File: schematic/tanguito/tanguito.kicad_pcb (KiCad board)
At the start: 2 copper layers, 10 parts, among them J1 Barrel_Jack, U2 L298N, U3 L298N

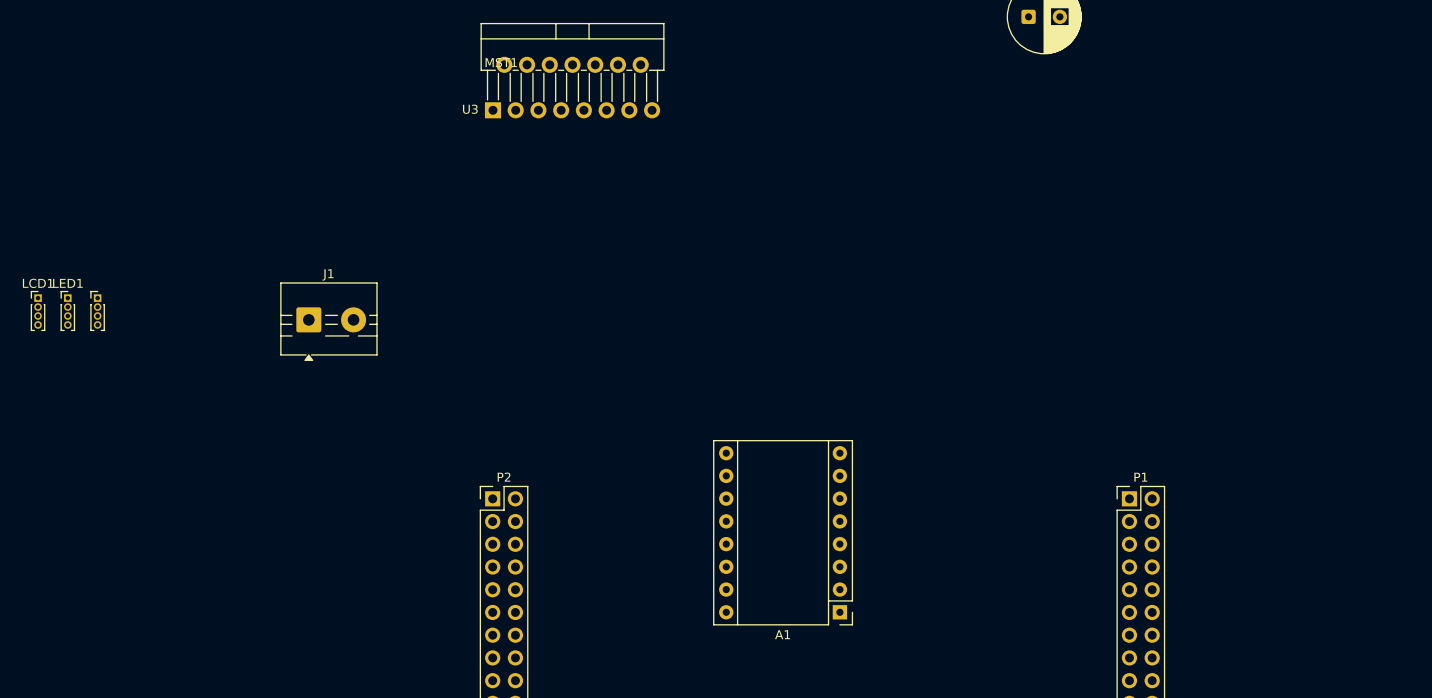
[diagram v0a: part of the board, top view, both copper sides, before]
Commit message: update: actualizando el esquematico y la huella del stepdwon (MP1584) y faltan concluir si usar pines macho o pads con tornillos en la PCB
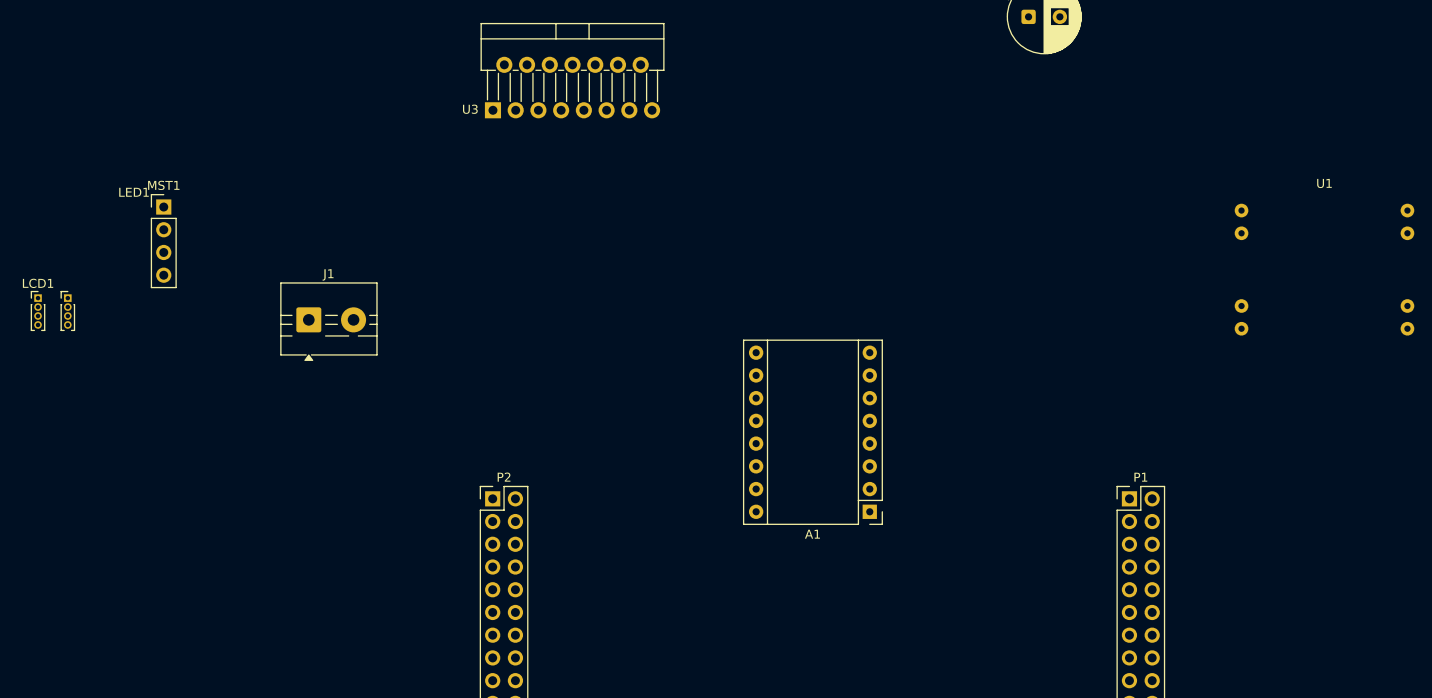
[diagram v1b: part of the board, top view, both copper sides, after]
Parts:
- added U1: MP1584_Module, MP1584_TodoMicro:MP1584_Module_TodoMicro_22x17, F.Cu at (190.0, 84.9)
- MST1: footprint Connector_PinHeader_1.00mm:PinHeader_1x04_P1.00mm_Vertical -> Connector_PinHeader_2.54mm:PinHeader_1x04_P2.54mm_Vertical
- moved MST1 12.6 mm to (60.2, 77.9)
- moved A1 11.7 mm to (139.1, 112.0)

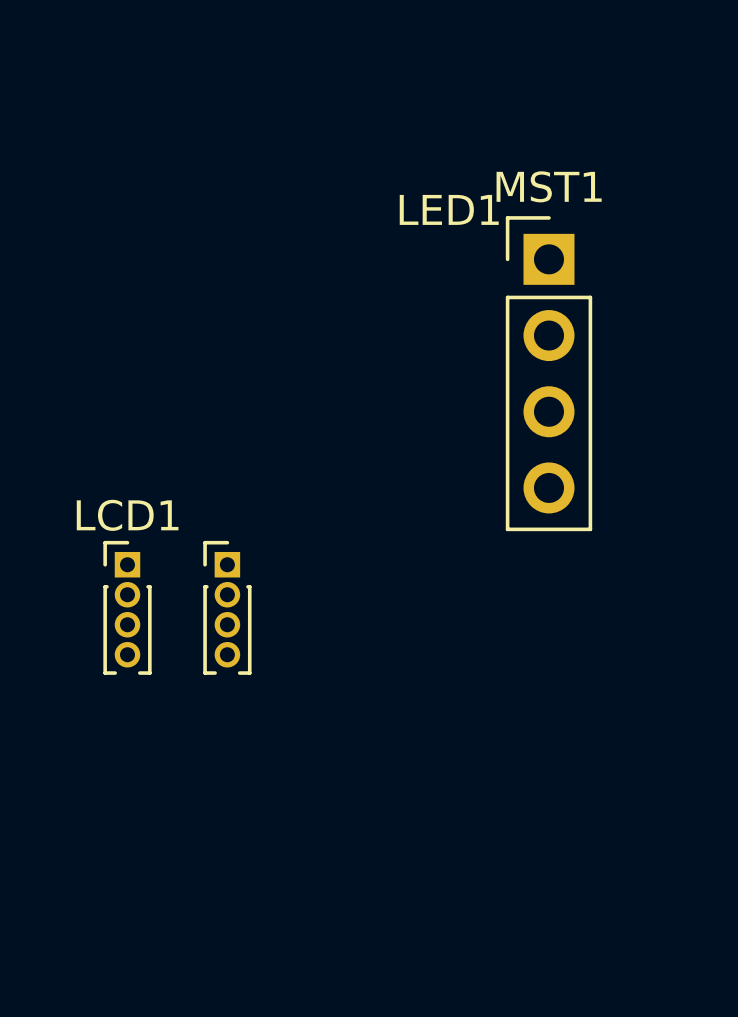
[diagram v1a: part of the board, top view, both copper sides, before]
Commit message: update: se cambiaron las huellas en el esquematico del LCD y del LED para que sean pads de 1x4 con pin patch de 2.54mm y se confirmo que el stepper ya cuenta con esa huella
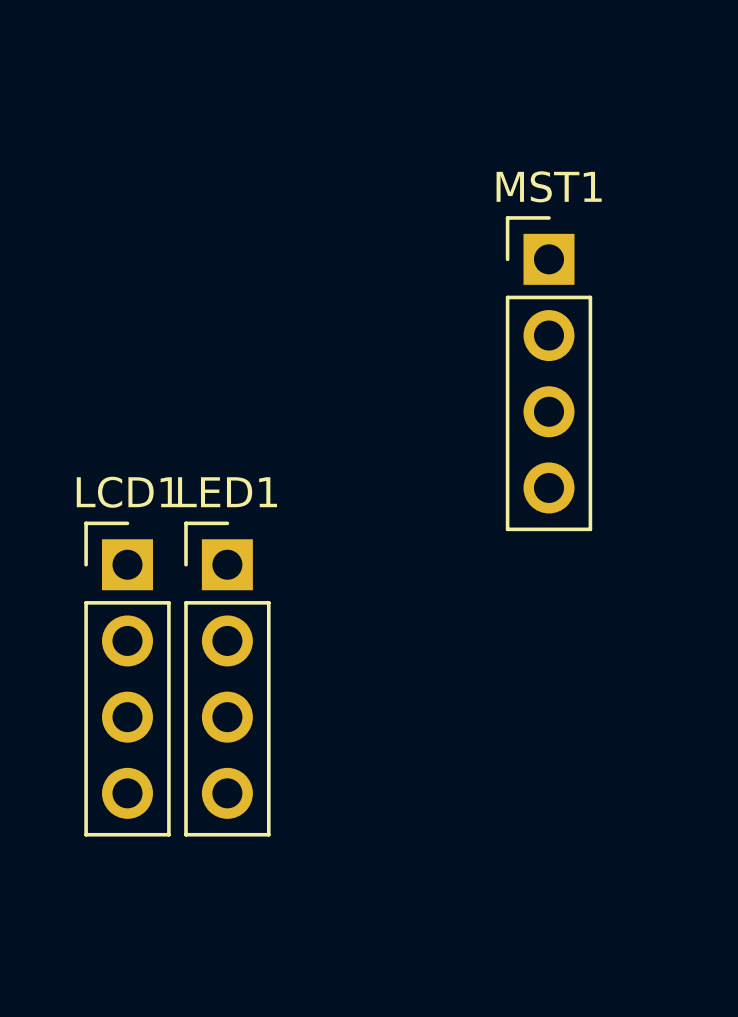
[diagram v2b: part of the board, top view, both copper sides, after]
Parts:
- LCD1, LED1: footprint Connector_PinHeader_1.00mm:PinHeader_1x04_P1.00mm_Vertical -> Connector_PinHeader_2.54mm:PinHeader_1x04_P2.54mm_Vertical

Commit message: diseño electrico y de PCB actualizados, pero faltan las pistas
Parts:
- added REF**: MountingHole_3.5mm_Pad, MountingHole:MountingHole_3.5mm_Pad, F.Cu at (245.6, 155.3)
- added REF**: MountingHole_3.5mm_Pad, MountingHole:MountingHole_3.5mm_Pad, F.Cu at (169.2, 155.3)
- added REF**: MountingHole_3.5mm_Pad, MountingHole:MountingHole_3.5mm_Pad, F.Cu at (169.2, 27.9)
- added REF**: MountingHole_3.5mm_Pad, MountingHole:MountingHole_3.5mm_Pad, F.Cu at (245.6, 27.9)
- J1: footprint TerminalBlock:TerminalBlock_MaiXu_MX126-5.0-02P_1x02_P5.00mm -> Connector_PinHeader_2.54mm:PinHeader_1x02_P2.54mm_Vertical
- U2: footprint Package_TO_SOT_THT:TO-220-15_P2.54x5.08mm_StaggerOdd_Lead4.58mm_Vertical -> Connector_PinHeader_2.54mm:PinHeader_1x10_P2.54mm_Vertical
- U3: footprint Package_TO_SOT_THT:TO-220-15_P2.54x5.08mm_StaggerOdd_Lead4.58mm_Vertical -> Connector_PinHeader_2.54mm:PinHeader_1x07_P2.54mm_Vertical
- moved J1 141.5 mm to (217.9, 92.7)
- moved LCD1 141.5 mm to (187.6, 90.3)
- moved LED1 141.5 mm to (191.0, 90.3)
- moved MST1 141.5 mm to (201.7, 80.1)
- moved U2 127.5 mm to (224.7, 48.7)
- moved A1 88.1 mm to (211.1, 61.2)
- moved U3 86.6 mm to (181.5, 48.0)
- moved P1 78.0 mm to (242.4, 86.4)
- moved P2 78.0 mm to (171.2, 86.4)
- moved C1 58.5 mm to (212.2, 75.5)
- moved U1 41.9 mm to (207.3, 123.1)
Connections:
- P1 pad 36: unconnected-(P1CONECTOR_P1-T_FL1-Pad36) -> /PWM0
- U2 pad 1: unconnected-(U2-SENSE_A-Pad1) -> GND
- U2 pad 2: /M1+ -> /M2-
- U2 pad 3: /M1- -> /M2+
- U2 pad 4: +12V -> /M1-
- U2 pad 5: /GPIO0 -> /M1+
- U2 pad 6: /PWM0 -> +12V
- U2 pad 7: GND -> /GPIO0
- U2 pad 9: unconnected-(U2-Vss-Pad9) -> /PWM0
- U3 pad 1: unconnected-(U3-SENSE_A-Pad1) -> GND
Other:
- board outline added: 85.8 x 137 mm
- rule pad_to_mask_clearance: 0 -> 0.0254

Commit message: pcb: updated
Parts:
- U2: footprint Connector_PinHeader_2.54mm:PinHeader_1x10_P2.54mm_Vertical -> Connector_PinHeader_2.54mm:PinHeader_1x12_P2.54mm_Vertical
- moved U2 98.3 mm to (244.9, 144.9), turned to -90 degrees
- moved U3 98.1 mm to (196.6, 144.9), turned to -90 degrees
- moved U1 66.8 mm to (221.0, 57.6), turned to -90 degrees
- moved J1 58.1 mm to (206.8, 35.6)
- moved LCD1 51.6 mm to (237.3, 104.2)
- moved C1 39.9 mm to (214.4, 35.6), turned to -90 degrees
- moved A1 36.1 mm to (191.6, 91.5)
- moved LED1 31.6 mm to (178.9, 119.5)
- moved MST1 6.35 mm to (201.7, 86.4), turned to 180 degrees
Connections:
- A1 pad 15: /GPIO2 -> /ENET_RXD1
- A1 pad 16: /GPIO3 -> /ENET_TXEN
- P1 pad 33: unconnected-(P1CONECTOR_P1-T_FL0-Pad33) -> /T_FIL0
- P1 pad 36: /PWM0 -> unconnected-(P1CONECTOR_P1-T_FL1-Pad36)
- P1 pad 39: unconnected-(P1CONECTOR_P1-T_COL0-Pad39) -> /T_COL0
- P2 pad 29: /GPIO0 -> unconnected-(P2CONECTOR_P2-GPIO0-Pad29)
- P2 pad 31: /GPIO2 -> unconnected-(P2CONECTOR_P2-GPIO2-Pad31)
- P2 pad 32: /GPIO1 -> unconnected-(P2CONECTOR_P2-GPIO1-Pad32)
- P2 pad 33: /GPIO4 -> unconnected-(P2CONECTOR_P2-GPIO4-Pad33)
- P2 pad 34: /GPIO3 -> unconnected-(P2CONECTOR_P2-GPIO3-Pad34)
- P2 pad 38: unconnected-(P2CONECTOR_P2-GPIO7-Pad38) -> /GPIO7
- P2 pad 4: unconnected-(P2CONECTOR_P2-RXD1-Pad4) -> /ENET_RXD1
- P2 pad 40: unconnected-(P2CONECTOR_P2-GPIO8-Pad40) -> /GPIO8
- P2 pad 6: unconnected-(P2CONECTOR_P2-TX_EN-Pad6) -> /ENET_TXEN
- U2 pad 7: /GPIO0 -> /T_COL0
- U2 pad 9: /PWM0 -> /PWM3
- U3 pad 5: /GPIO4 -> /GPIO7
- U3 pad 6: /PWM4 -> /GPIO8
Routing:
- net +12V: track 0.00 -> 412.6 mm
- net GND: track 0.00 -> 402.9 mm
- net +5V: track 0.00 -> 147.0 mm
- net /T_FIL0: track 0.00 -> 42.5 mm
- net /PWM4: track 0.00 -> 37.4 mm
- net /PWM3: track 0.00 -> 29.8 mm
- net /GPIO7: track 0.00 -> 24.7 mm
- net /MST B1: track 0.00 -> 23.9 mm
- net /T_COL0: track 0.00 -> 22.2 mm
- net /GPIO8: track 0.00 -> 19.6 mm
- net /MST A2: track 0.00 -> 12.0 mm
- net /MST A1: track 0.00 -> 11.6 mm
- net /MST B2: track 0.00 -> 10.2 mm
- net /GPIO5: track 0.00 -> 10.2 mm
- net /I2C_SCL: track 0.00 -> 5.12 mm
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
